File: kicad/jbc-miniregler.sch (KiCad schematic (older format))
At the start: 23 parts, among them SW1 UP, SW2 DOWN, SW3 ENTER, SW4 BACK, U1 OLED-128x32-Module, X1 POWER, X2 COM, X3 Lötkolben

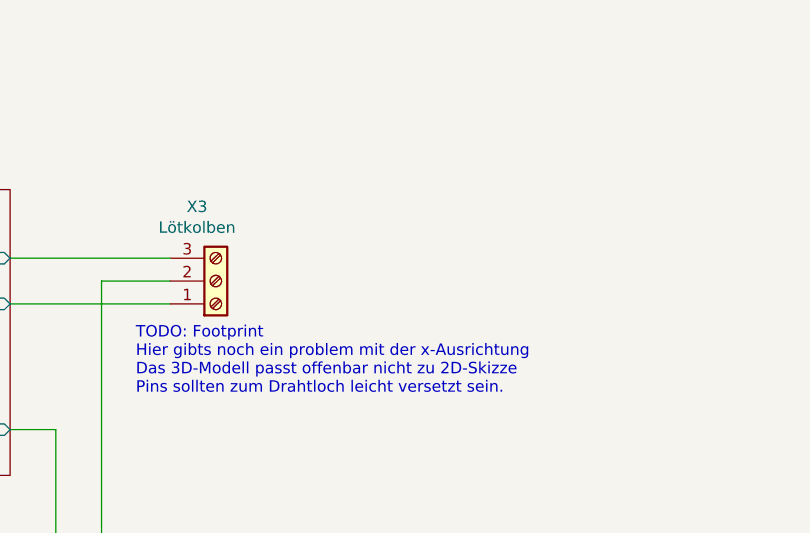
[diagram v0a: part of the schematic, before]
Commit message: Notizen, Kabelbelegung, Alternativbestückung
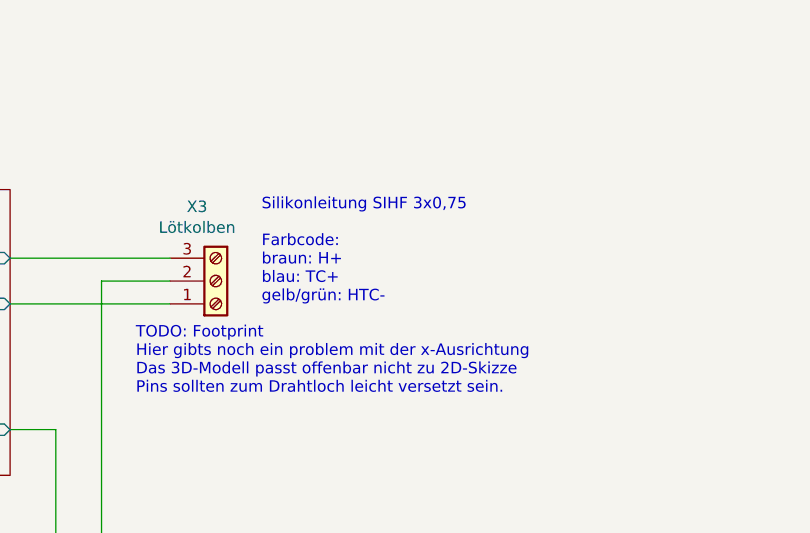
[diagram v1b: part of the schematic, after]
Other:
- note added: "Silikonleitung SIHF 3x0,75\n\nFarbcode:\nbraun: H+\nblau: TC+\ngelb/grün: HTC-"
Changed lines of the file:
@@
 	1    0    0    -1
 $EndComp
+Text Notes 8750 1950 0    50   ~ 0
+Silikonleitung SIHF 3x0,75\n\nFarbcode:\nbraun: H+\nblau: TC+\ngelb/grün: HTC-
 $EndSCHEMATC
